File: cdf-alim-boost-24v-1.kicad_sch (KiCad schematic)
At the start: 21 parts, among them J1 Conn_01x02, J2 Conn_01x02, Q1 IRF8736PbF, Q2 IRF8736PbF

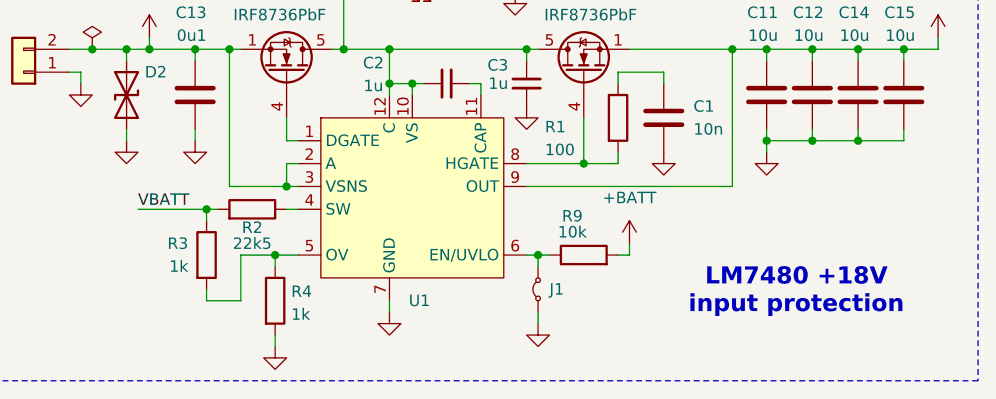
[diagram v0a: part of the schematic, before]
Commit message: schem: limit vinmax to 23V
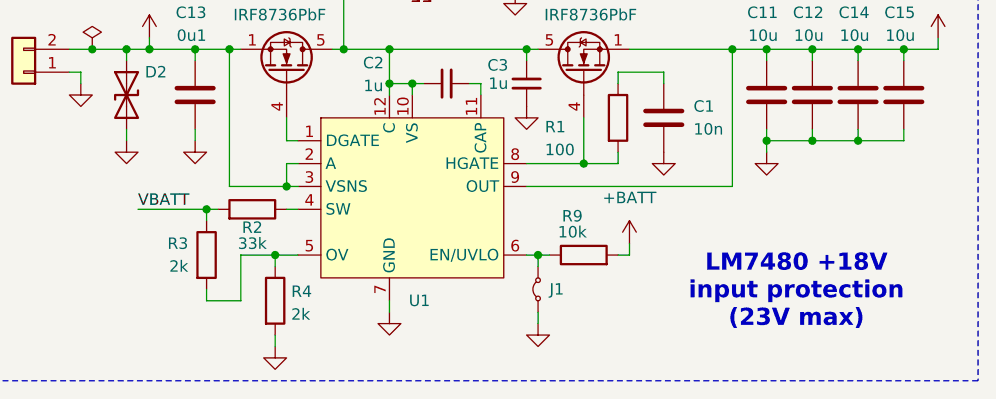
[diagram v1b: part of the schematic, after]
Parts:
- R2: value 22k5 -> 33k
- R3, R4: value 1k -> 2k
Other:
- note added: "LM7480 +18V input protection (23V max)"
- note removed: "LM7480 +18V input protection"
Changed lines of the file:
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@@
 		)
 	)
-	(text "LM7480 +18V\ninput protection"
+	(text "LM7480 +18V\ninput protection\n(23V max)"
 		(exclude_from_sim no)
 		(at 106.172 56.134 0)
@@
 			)
 		)
-		(property "Value" "1k"
+		(property "Value" "2k"
 			(at 38.608 53.34 0)
 			(show_name no)
@@
 			)
 		)
-		(property "Value" "1k"
+		(property "Value" "2k"
 			(at 50.038 58.674 0)
 			(show_name no)
@@
 			)
 		)
-		(property "Value" "22k5"
+		(property "Value" "33k"
 			(at 45.72 50.8 90)
 			(show_name no)

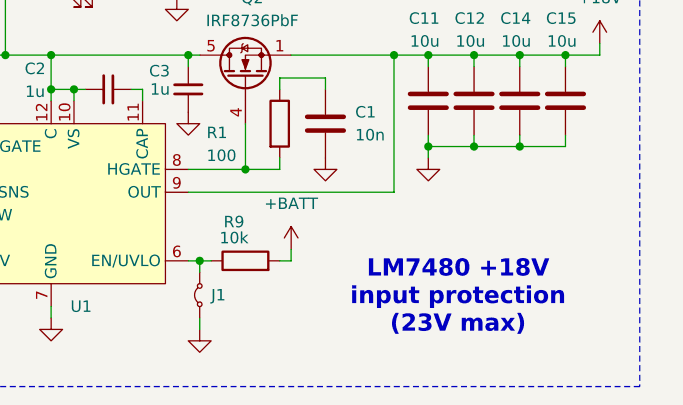
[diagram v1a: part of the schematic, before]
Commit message: schem: add lm7480 14v uvlo
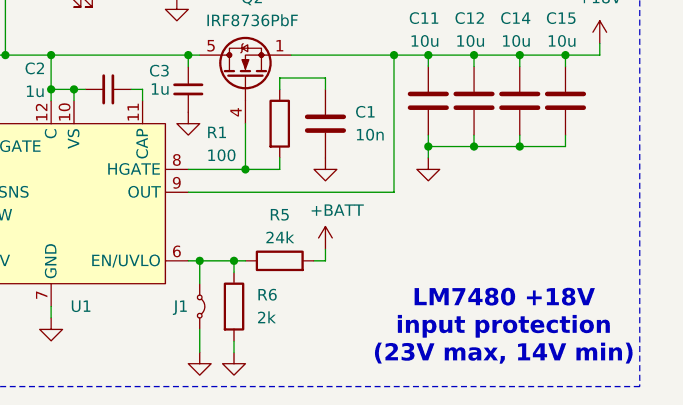
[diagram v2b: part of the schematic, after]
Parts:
- removed R9: 10k, Resistor_SMD:R_0402_1005Metric, symbol Device:R
- added R5: 24k, Package_SO:Texas_PWP0020A, symbol Device:R
- added R6: 2k, symbol Device:R
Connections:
- net +BATT: now also R5.2
- net GND: now also R6.2
- net at J1.2 (B), U1.6 (EN/UVLO): now also R5.1, R6.1
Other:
- note added: "LM7480 +18V input protection (23V max, 14V min)"
- note removed: "LM7480 +18V input protection (23V max)"

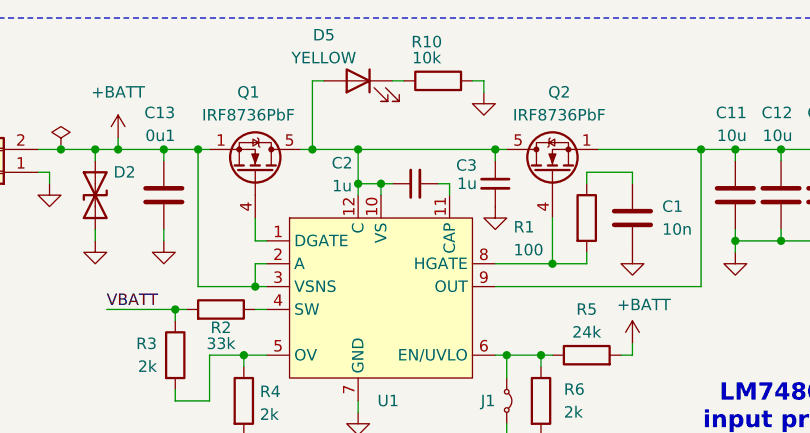
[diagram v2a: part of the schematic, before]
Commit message: schem: update lm7480 mosfets
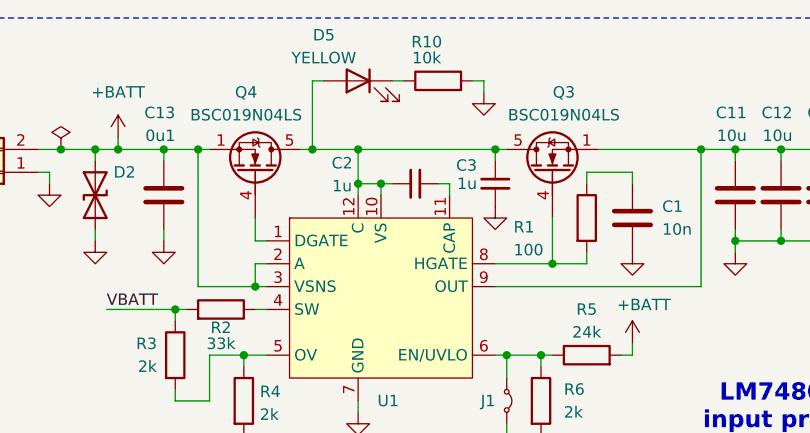
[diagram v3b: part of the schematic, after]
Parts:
- removed Q1, Q2: IRF8736PbF, Package_SO:SOIC-8_3.9x4.9mm_P1.27mm, symbol Transistor_FET:IRF8721PBF-1
- added Q3, Q4: BSC019N04LS, Package_TO_SOT_SMD:TDSON-8-1, symbol Transistor_FET:CSD18501Q5A
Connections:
- net +18V: now also Q3.1 (S), Q3.2 (S), Q3.3 (S)
- net +BATT: now also Q4.1 (S), Q4.2 (S), Q4.3 (S)
- net at U1.1 (DGATE): now also Q4.4 (G)
- net at C2.2, C3.2, D5.2 (A)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: now also Q3.5 (D), Q4.5 (D)
- net at R1.2, U1.8 (HGATE): now also Q3.4 (G)
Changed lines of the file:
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@@
 	)
 	(symbol
-		(lib_id "Transistor_FET:IRF8721PBF-1")
-		(at 49.53 31.75 270)
-		(mirror x)
-		(unit 1)
-		(body_style 1)
-		(exclude_from_sim no)
-		(in_bom yes)
-		(on_board yes)
-		(in_pos_files yes)
-		(dnp no)
-		(property "Reference" "Q1"
-			(at 48.768 22.86 90)
-			(show_name no)
-			(do_not_autoplace no)
-			(effects
-				(font
-					(size 1.27 1.27)
-				)
-			)
-		)
-		(property "Value" "IRF8736PbF"
-			(at 48.768 25.4 90)
-			(show_name no)
-			(do_not_autoplace no)
-			(effects
-				(font
-					(size 1.27 1.27)
-				)
-			)
-		)
-		(property "Footprint" "Package_SO:SOIC-8_3.9x4.9mm_P1.27mm"
-			(at 47.625 26.67 0)
-			(hide yes)
-			(show_name no)
-			(do_not_autoplace no)
-			(effects
-				(font
-					(size 1.27 1.27)
-					(italic yes)
-				)
-				(justify left)
-			)
-		)
-		(property "Datasheet" "http://www.irf.com/product-info/datasheets/data/irf8721pbf-1.pdf"
-			(at 45.72 26.67 0)
-			(hide yes)
-			(show_name no)
-			(do_not_autoplace no)
-			(effects
-				(font
-					(size 1.27 1.27)
-				)
-				(justify left)
-			)
-		)
-		(property "Description" "14A Id, 30V Vds, HEXFET N-Channel MOSFET, SO-8"
-			(at 49.53 31.75 0)
-			(hide yes)
-			(show_name no)
-			(do_not_autoplace no)
-			(effects
-				(font
-					(size 1.27 1.27)
-				)
-			)
-		)
-		(pin "8"
-		)
-		(pin "2"
-		)
-		(pin "4"
-		)
-		(pin "7"
-		)
-		(pin "1"
-		)
-		(pin "5"
-		)
-		(pin "3"
-		)
-		(pin "6"
-		)
-		(instances
-			(project "cdf-alim-boost-24v-1"
-				(path "/c1d68e1e-31aa-4338-bfd5-3714fe43b2c6"
-					(reference "Q1")
-					(unit 1)
-				)
-			)
-		)
-	)
-	(symbol
 		(lib_id "power:GND")
 		(at 31.75 39.37 0)
@@
 	)
 	(symbol
-		(lib_id "Transistor_FET:IRF8721PBF-1")
-		(at 82.55 31.75 90)
-		(unit 1)
-		(body_style 1)
-		(exclude_from_sim no)
-		(in_bom yes)
-		(on_board yes)
-		(in_pos_files yes)
-		(dnp no)
-		(property "Reference" "Q2"
-			(at 83.312 22.86 90)
-			(show_name no)
-			(do_not_autoplace no)
-			(effects
-				(font
-					(size 1.27 1.27)
-				)
-			)
-		)
-		(property "Value" "IRF8736PbF"
-			(at 83.312 25.4 90)
-			(show_name no)
-			(do_not_autoplace no)
-			(effects
-				(font
-					(size 1.27 1.27)
-				)
-			)
-		)
-		(property "Footprint" "Package_SO:SOIC-8_3.9x4.9mm_P1.27mm"
-			(at 84.455 26.67 0)
-			(hide yes)
-			(show_name no)
-			(do_not_autoplace no)
-			(effects
-				(font
-					(size 1.27 1.27)
-					(italic yes)
-				)
-				(justify left)
-			)
-		)
-		(property "Datasheet" "http://www.irf.com/product-info/datasheets/data/irf8721pbf-1.pdf"
-			(at 86.36 26.67 0)
-			(hide yes)
-			(show_name no)
-			(do_not_autoplace no)
-			(effects
-				(font
-					(size 1.27 1.27)
-				)
-				(justify left)
-			)
-		)
-		(property "Description" "14A Id, 30V Vds, HEXFET N-Channel MOSFET, SO-8"
-			(at 82.55 31.75 0)
-			(hide yes)
-			(show_name no)
-			(do_not_autoplace no)
-			(effects
-				(font
-					(size 1.27 1.27)
-				)
-			)
-		)
-		(pin "8"
-		)
-		(pin "2"
-		)
-		(pin "4"
-		)
-		(pin "7"
-		)
-		(pin "1"
-		)
-		(pin "5"
-		)
-		(pin "3"
-		)
-		(pin "6"
-		)
-		(instances
-			(project "cdf-alim-boost-24v-1"
-				(path "/c1d68e1e-31aa-4338-bfd5-3714fe43b2c6"
-					(reference "Q2")
-					(unit 1)
-				)
-			)
-		)
-	)
-	(symbol
 		(lib_id "power:GND")
 		(at 102.87 40.64 0)
@@
 	)
 	(symbol
+		(lib_id "Transistor_FET:CSD18501Q5A")
+		(at 82.55 31.75 90)
+		(unit 1)
+		(body_style 1)
+		(exclude_from_sim no)
+		(in_bom yes)
+		(on_board yes)
+		(in_pos_files yes)
+		(dnp no)
+		(property "Reference" "Q3"
+			(at 83.82 22.86 90)
+			(show_name no)
+			(do_not_autoplace no)
+			(effects
+				(font
+					(size 1.27 1.27)
+				)
+			)
+		)
+		(property "Value" "BSC019N04LS"
+			(at 83.82 25.4 90)
+			(show_name no)
+			(do_not_autoplace no)
+			(effects
+				(font
+					(size 1.27 1.27)
+				)
+			)
+		)
+		(property "Footprint" "Package_TO_SOT_SMD:TDSON-8-1"
+			(at 84.455 26.67 0)
+			(hide yes)
+			(show_name no)
+			(do_not_autoplace no)
+			(effects
+				(font
+					(size 1.27 1.27)
+					(italic yes)
+				)
+				(justify left)
+			)
+		)
+		(property "Datasheet" "http://www.ti.com/lit/gpn/csd18501q5a"
+			(at 86.36 26.67 0)
+			(hide yes)
+			(show_name no)
+			(do_not_autoplace no)
+			(effects
+				(font
+					(size 1.27 1.27)
+				)
+				(justify left)
+			)
+		)
+		(property "Description" "100A Id, 40V Vds, NexFET N-Channel Power MOSFET, 3.2mOhm Ron, 42nC Qg(typ), SON8 5x6mm"
+			(at 82.55 31.75 0)
+			(hide yes)
+			(show_name no)
+			(do_not_autoplace no)
+			(effects
+				(font
+					(size 1.27 1.27)
+				)
+			)
+		)
+		(pin "2"
+		)
+		(pin "1"
+		)
+		(pin "4"
+		)
+		(pin "3"
+		)
+		(pin "5"
+		)
+		(instances
+			(project "cdf-alim-boost-24v-1"
+				(path "/c1d68e1e-31aa-4338-bfd5-3714fe43b2c6"
+					(reference "Q3")
+					(unit 1)
+				)
+			)
+		)
+	)
+	(symbol
 		(lib_id "Device:C")
 		(at 91.44 36.83 0)
@@
 					(unit 1)
 				)
+			)
+		)
+	)
+	(symbol
+		(lib_id "Transistor_FET:CSD18501Q5A")
+		(at 49.53 31.75 270)
+		(mirror x)
+		(unit 1)
+		(body_style 1)
+		(exclude_from_sim no)
+		(in_bom yes)
+		(on_board yes)
+		(in_pos_files yes)
+		(dnp no)
+		(property "Reference" "Q4"
+			(at 48.514 22.86 90)
+			(show_name no)
+			(do_not_autoplace no)
+			(effects
+				(font
+					(size 1.27 1.27)
+				)
+			)
+		)
+		(property "Value" "BSC019N04LS"
+			(at 48.514 25.4 90)
+			(show_name no)
+			(do_not_autoplace no)
+			(effects
+				(font
+					(size 1.27 1.27)
+				)
+			)
+		)
+		(property "Footprint" "Package_TO_SOT_SMD:TDSON-8-1"
+			(at 47.625 26.67 0)
+			(hide yes)
+			(show_name no)
+			(do_not_autoplace no)
+			(effects
+				(font
+					(size 1.27 1.27)
+					(italic yes)
+				)
+				(justify left)
+			)
+		)
+		(property "Datasheet" "http://www.ti.com/lit/gpn/csd18501q5a"
+			(at 45.72 26.67 0)
+			(hide yes)
+			(show_name no)
+			(do_not_autoplace no)
+			(effects
+				(font
+					(size 1.27 1.27)
+				)
+				(justify left)
+			)
+		)
+		(property "Description" "100A Id, 40V Vds, NexFET N-Channel Power MOSFET, 3.2mOhm Ron, 42nC Qg(typ), SON8 5x6mm"
+			(at 49.53 31.75 0)
+			(hide yes)
+			(show_name no)
+			(do_not_autoplace no)
+			(effects
+				(font
+					(size 1.27 1.27)
+				)
+			)
+		)
+		(pin "2"
+		)
+		(pin "1"
+		)
+		(pin "4"
+		)
+		(pin "3"
+		)
+		(pin "5"
+		)
+		(instances
+			(project "cdf-alim-boost-24v-1"
+				(path "/c1d68e1e-31aa-4338-bfd5-3714fe43b2c6"
+					(reference "Q4")
+					(unit 1)
+				)

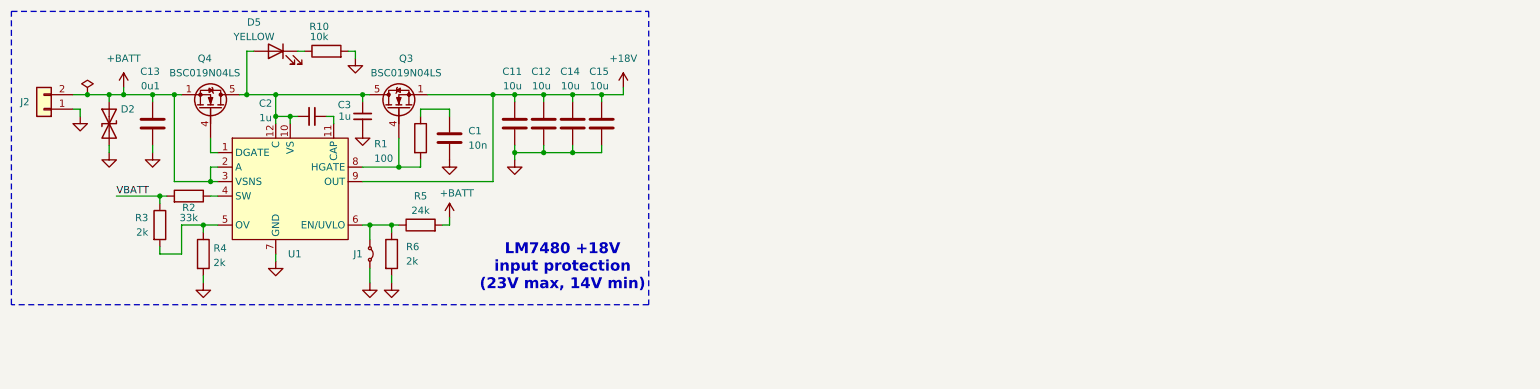
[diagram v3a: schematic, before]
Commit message: schem: add LM5122 24V 10A BOOST SMPS
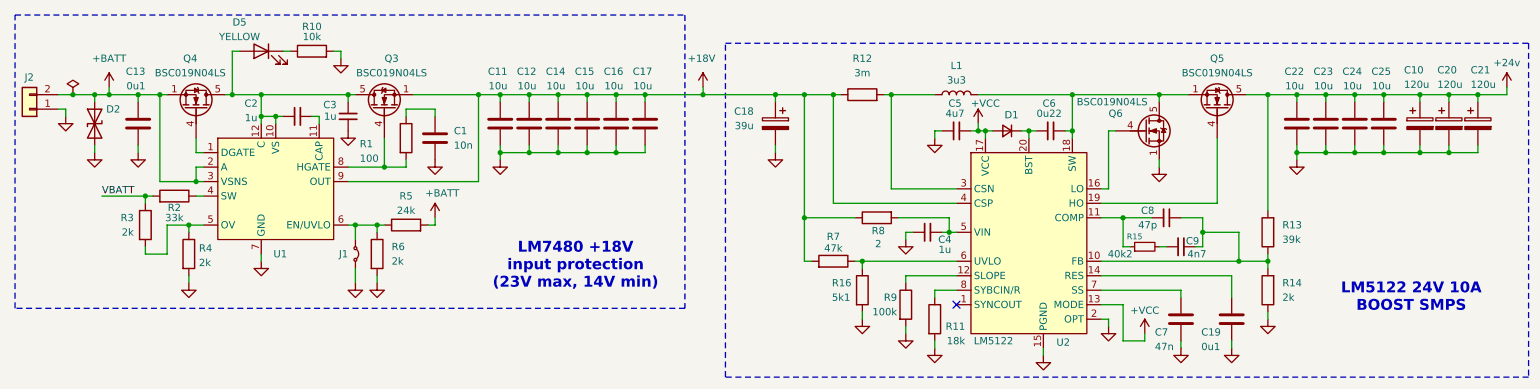
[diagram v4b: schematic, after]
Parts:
- added C10, C20, C21: 120u, symbol Device:C_Polarized
- added C16, C17, C22, C23, C24, C25: 10u, Capacitor_SMD:C_1206_3216Metric, symbol Device:C
- added C18: 39u, Capacitor_SMD:CP_Elec_8x6.9, symbol Device:C_Polarized
- added C19: 0u1, Capacitor_SMD:C_0402_1005Metric, symbol Device:C
- added C4: 1u, symbol Device:C_Small
- added C5: 4u7, symbol Device:C_Small
- added C6: 0u22, symbol Device:C_Small
- added C7: 47n, symbol Device:C
- added C8: 47p, symbol Device:C_Small
- added C9: 4n7, symbol Device:C_Small
- added D1: D_Small, symbol Device:D_Small
- added L1: 3u3, Inductor_SMD:L_Sunlord_MWSA1205S-3R3, symbol Device:L
- added Q5, Q6: BSC019N04LS, Package_TO_SOT_SMD:TDSON-8-1, symbol Transistor_FET:CSD18501Q5A
- added R11: 18k, symbol Device:R
- added R12: 3m, Resistor_SMD:R_1020_2550Metric, symbol Device:R
- added R13: 39k, symbol Device:R
- added R14: 2k, symbol Device:R
- added R15: 40k2, symbol Device:R_Small
- added R16: 5k1, Resistor_SMD:R_0402_1005Metric, symbol Device:R
- added R7: 47k, symbol Device:R
- added R8: 2, symbol Device:R
- added R9: 100k, symbol Device:R
- added U2: LM5122, Package_SO:Texas_PWP0020A, symbol GLCS:LM5122
- C11, C12, C14, C15: footprint Capacitor_SMD:C_0805_2012Metric -> Capacitor_SMD:C_1206_3216Metric; JLCPCB Part # C440198 -> C13585; Manufacturer Murata -> Samsung Electro-Mechanics; Manufacturer Part Number GRM21BR61H106KE43L -> CL31A106KBHNNNE
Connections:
- net +18V: now also C16.1, C17.1, C18.1, R12.1, R7.2, R8.1, U2.4 (CSP)
- net GND renamed AGND
- net AGND: now also C10.2, C16.2, C17.2, C18.2, C19.2, C20.2, C21.2, C22.2, C23.2, C24.2, C25.2, C4.1, C5.2, C7.2, Q6.1 (S), Q6.2 (S), Q6.3 (S), R11.2, R14.1, R16.2, R9.2, U2.15 (PGND), U2.2 (OPT), U2.21 (EP), U2.9 (AGND)
- new net: C19.1, U2.14 (RES)
- new net: C8.2, C9.2, R13.1, R14.2, U2.10 (FB)
- new net: C8.1, R15.1, U2.11 (COMP)
- new net: R9.1, U2.12 (SLOPE)
- new net: Q6.4 (G), U2.16 (LO)
- new net: C6.1, L1.2, Q5.1 (S), Q5.2 (S), Q5.3 (S), Q6.5 (D), U2.18 (SW)
- new net: Q5.4 (G), U2.19 (HO)
- new net: C6.2, D1.1 (K), U2.20 (BST)
- new net: L1.1, R12.2, U2.3 (CSN)
- new net: C4.2, R8.2, U2.5 (VIN)
- new net: R16.1, R7.1, U2.6 (UVLO)
- new net: C7.1, U2.7 (SS)
- new net: R11.1, U2.8 (SYBCIN/R)
- new net: C9.1, R15.2
- new net +24v: C10.1, C20.1, C21.1, C22.1, C23.1, C24.1, C25.1, Q5.5 (D), R13.2
- new net +VCC: C5.1, D1.2 (A), U2.13 (MODE), U2.17 (VCC)
- no-connect marks 0 -> 1
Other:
- note added: "LM5122 24V 10A BOOST SMPS"
- moved on the sheet: C1, C11, C13, C2, C3, D2, D5, J1, J2, Q3, Q4, R1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
